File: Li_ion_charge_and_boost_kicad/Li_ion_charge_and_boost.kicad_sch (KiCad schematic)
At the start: 10 parts, among them U1 TP4056, U2 Type_C_6_pin

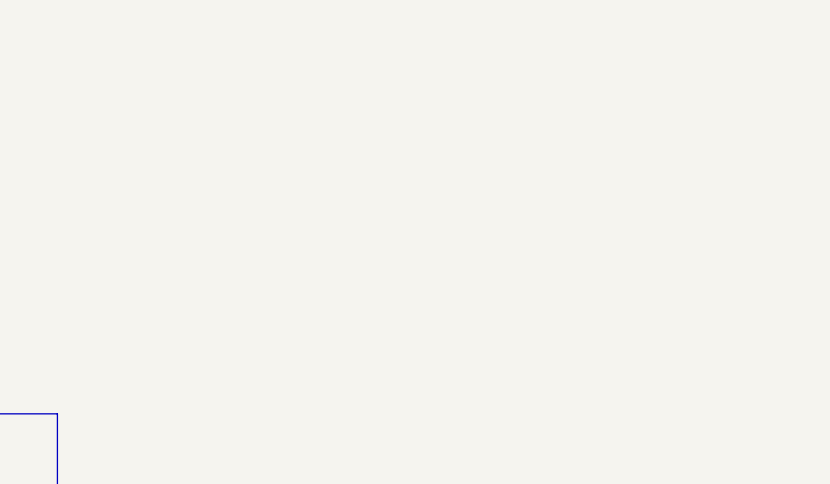
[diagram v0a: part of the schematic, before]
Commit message: DW01A included
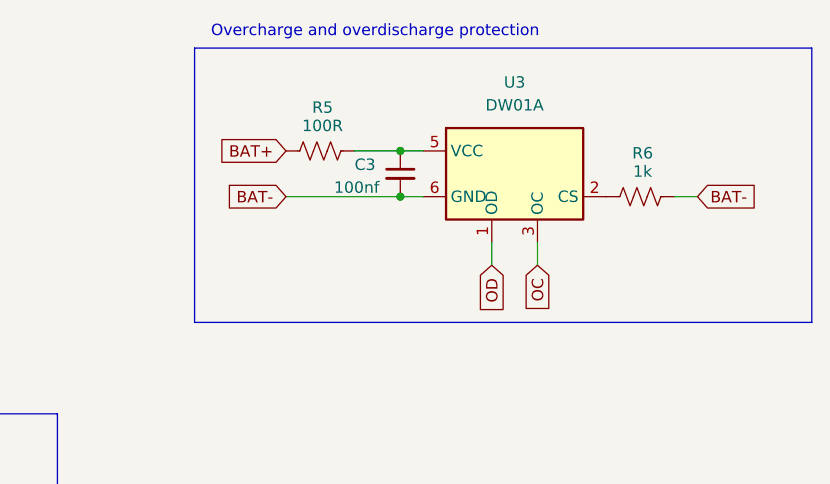
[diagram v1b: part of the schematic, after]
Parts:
- added C3: 100nf, symbol Device:C_Small
- added R5: 100R, symbol Device:R_US
- added R6: 1k, symbol Device:R_US
- added U3: DW01A, Package_TO_SOT_SMD:SOT-23-6, symbol Battery_Management:DW01A
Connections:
- net BAT+: now also R5.1
- new net: C3.1, R5.2, U3.5 (VCC)
- new net: R6.1, U3.2 (CS)
- new net BAT-: C3.2, R6.2, U3.6 (GND)
- new net OC: U3.3 (OC)
- new net OD: U3.1 (OD)
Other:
- note added: "Overcharge and overdischarge protection"

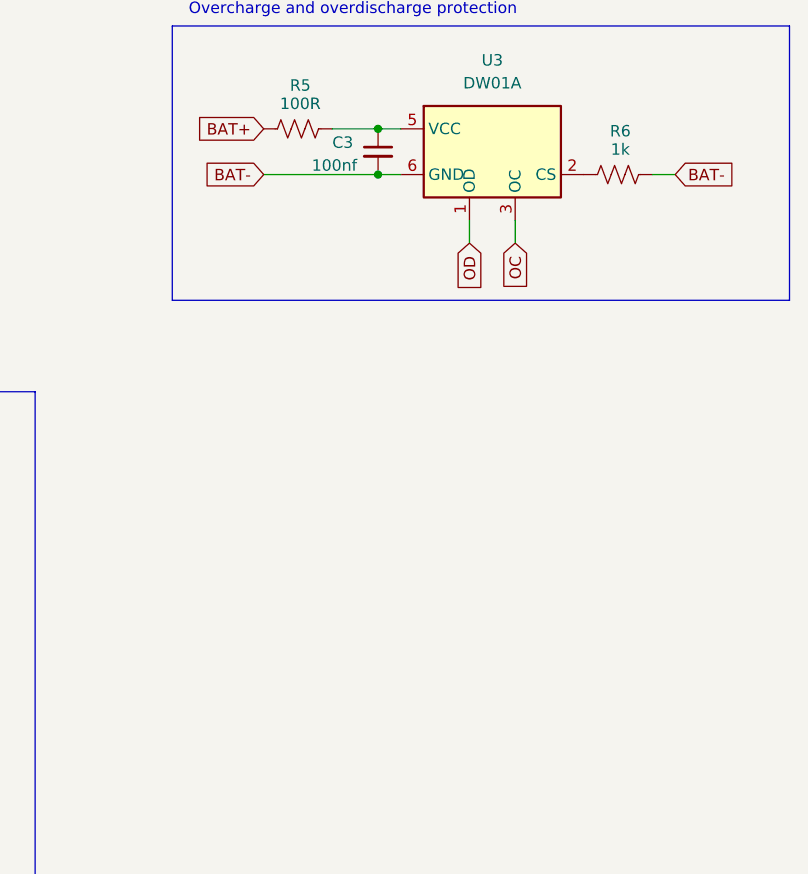
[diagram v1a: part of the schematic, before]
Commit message: Mosfet switch added
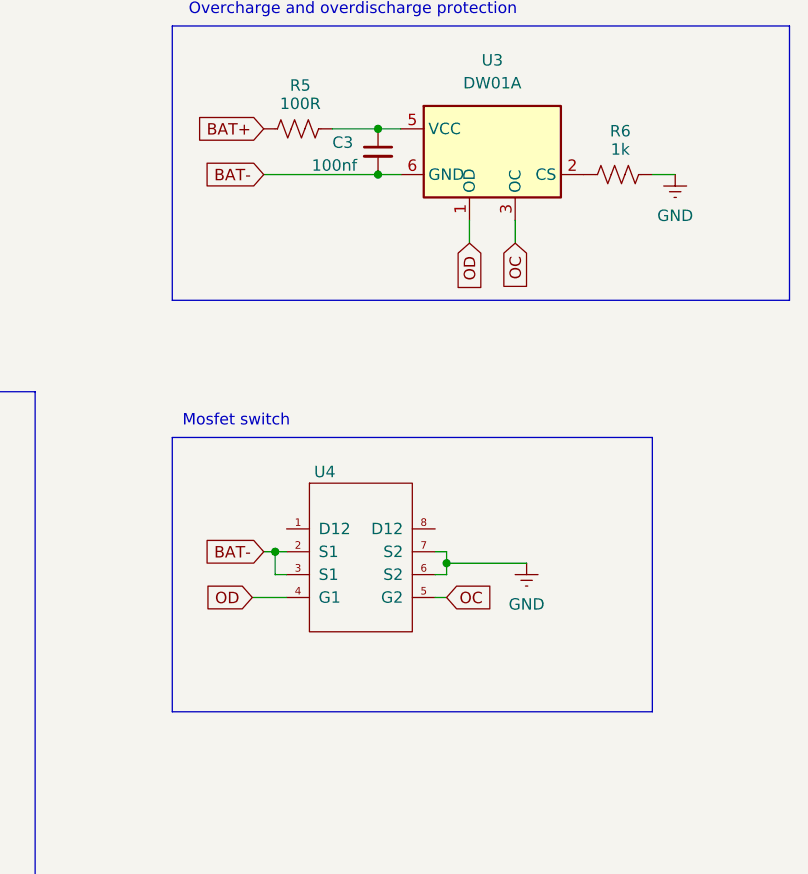
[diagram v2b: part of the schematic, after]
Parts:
- added U4: ~, symbol My_Library:FS8205A
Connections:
- net BAT-: now also U4.2 (S1), U4.3 (S1); no longer R6.2
- net GND: now also R6.2, U4.6 (S2), U4.7 (S2)
- net OC: now also U4.5 (G2)
- net OD: now also U4.4 (G1)
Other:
- note added: "Mosfet switch"

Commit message: Li ion charger completed
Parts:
- U4: footprint (none) -> My Library:FS8205A
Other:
- note added: "Li ion Charger"
- moved on the sheet: C3, R5, R6, U2, U3, U4

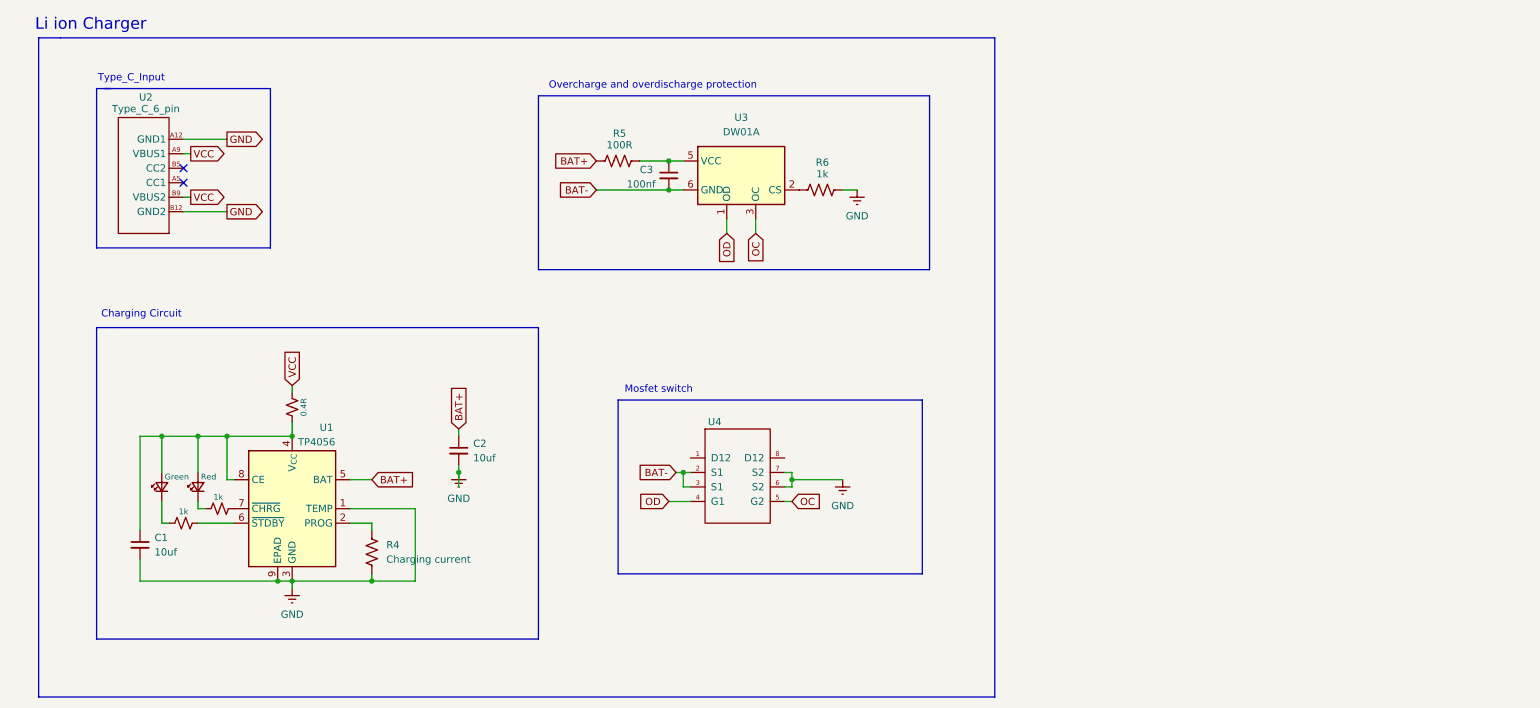
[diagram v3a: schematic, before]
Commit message: Boost converter added
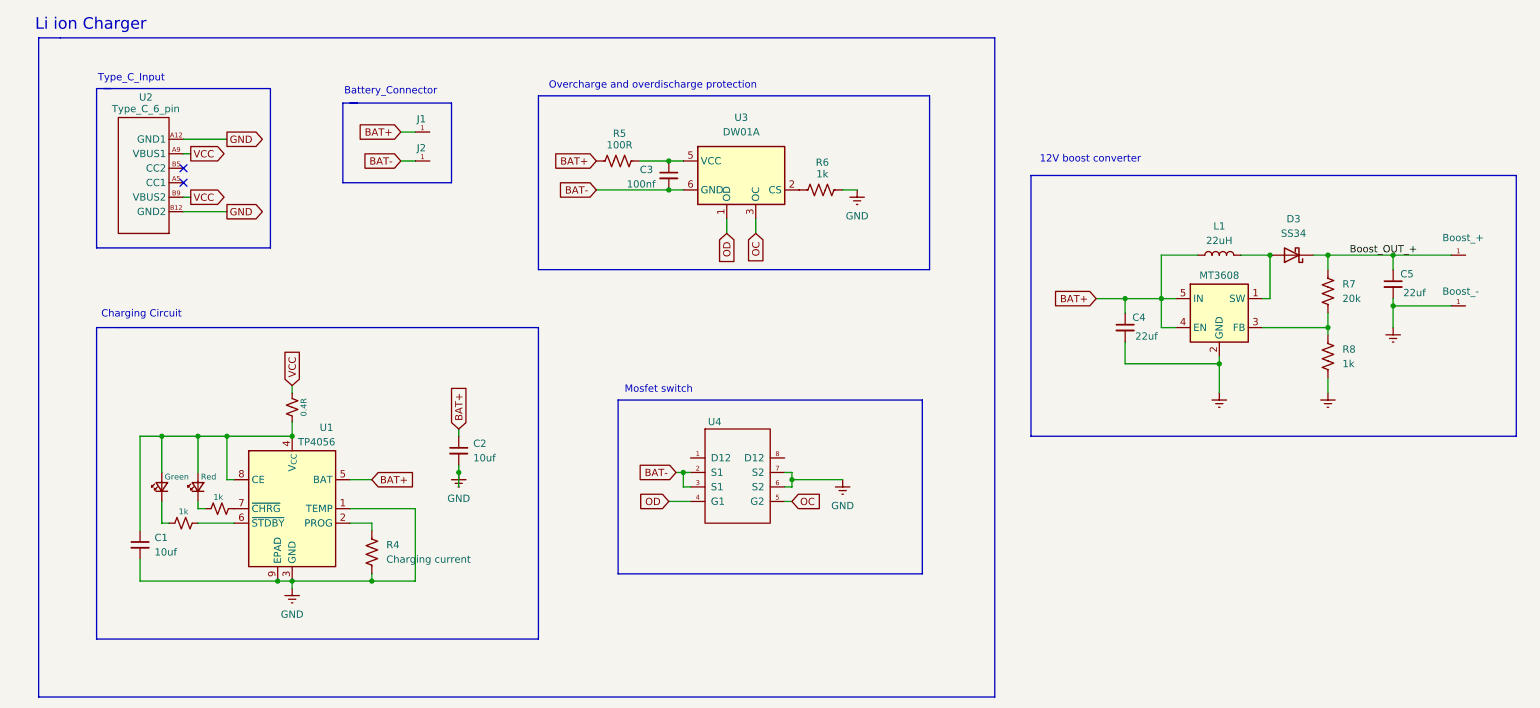
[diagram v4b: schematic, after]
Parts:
- added C4, C5: 22uf, symbol Device:C_Small
- added D3: SS34, Diode_SMD:D_SMA, symbol Diode:SS34
- added J1, J2: ~, symbol My_Library:Power_Connector
- added J3: Boost_+, symbol My_Library:Power_Connector
- added J4: Boost_-, symbol My_Library:Power_Connector
- added L1: 22uH, symbol Device:L
- added R7: 20k, symbol Device:R_US
- added R8: 1k, symbol Device:R_US
- added U5: MT3608, Package_TO_SOT_SMD:SOT-23-6, symbol Regulator_Switching:MT3608
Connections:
- net BAT+: now also C4.1, J1.1, L1.1, U5.4 (EN), U5.5 (IN)
- net BAT-: now also J2.1
- net GND: now also C4.2, C5.2, J4.1, R8.2, U5.2 (GND)
- new net: R7.2, R8.1, U5.3 (FB)
- new net: D3.2 (A), L1.2, U5.1 (SW)
- new net Boost_OUT_+: C5.1, D3.1 (K), J3.1, R7.1
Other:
- note added: "12V boost converter"
- note added: "Battery_Connector"

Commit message: Charging current and Inductor yet to confirm
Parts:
- R4: value Charging current -> 1.2k ( charging Current )
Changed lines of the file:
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@@
 	)
 	(junction
-		(at 93.98 105.41)
-		(diameter 0)
-		(color 0 0 0 0)
-	)
-	(junction
 		(at 257.81 67.31)
 		(diameter 0)
@@
 	(wire
 		(pts
-			(xy 93.98 105.41) (xy 93.98 107.95)
-		)
-		(stroke
-			(width 0)
-			(type default)
-		)
-	)
-	(wire
-		(pts
 			(xy 93.98 97.79) (xy 93.98 99.06)
 		)
@@
 		(on_board yes)
 		(dnp no)
-		(fields_autoplaced yes)
 		(property "Reference" "R4"
 			(at 81.28 118.1099 0)
@@
 			)
 		)
-		(property "Value" "Charging current"
-			(at 81.28 120.6499 0)
+		(property "Value" "1.2k   ( charging Current )"
+			(at 81.026 120.65 0)
 			(effects
 				(font

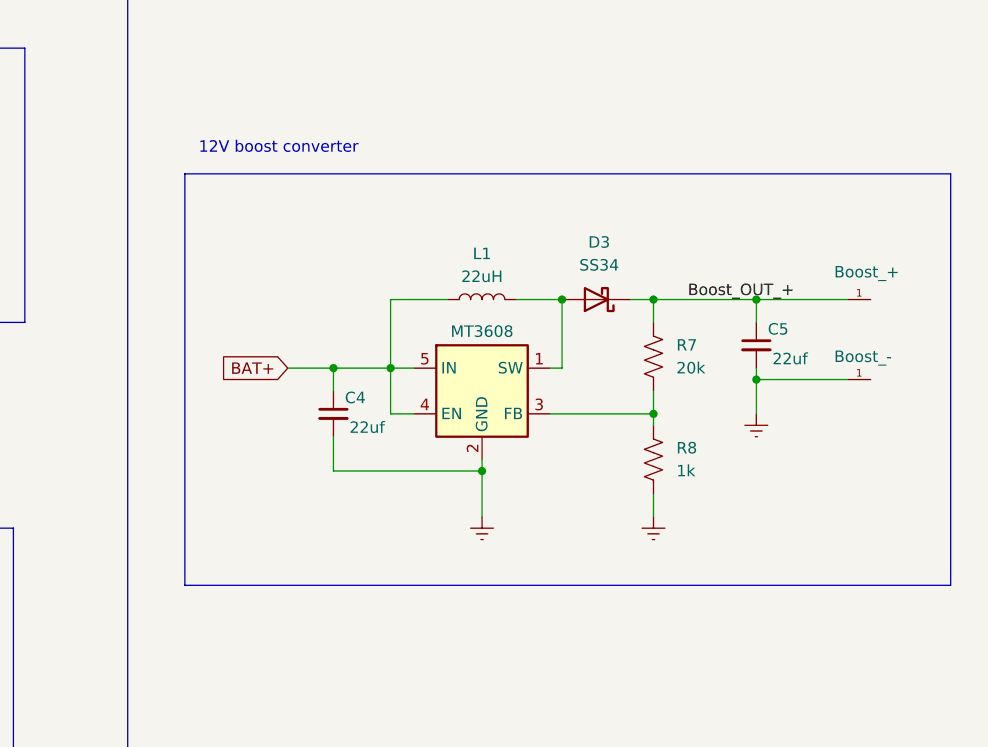
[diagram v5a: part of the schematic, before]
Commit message: switch input, microcontroller input and 2nd connector output
Switch to control the boost converter manually. Micorocontroller input to control automatically and 2nd output connector for more connections.
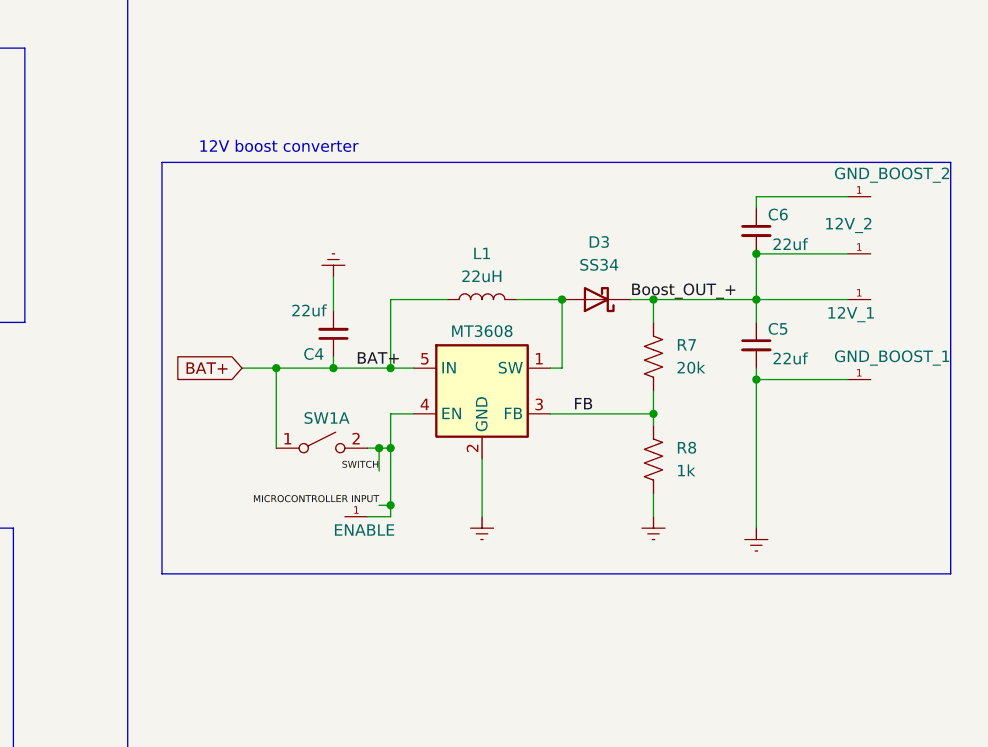
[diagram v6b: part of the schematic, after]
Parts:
- added C6: 22uf, symbol Device:C_Small
- added J5: ENABLE, symbol My_Library:Power_Connector
- added J6: 12V_2, symbol My_Library:Power_Connector
- added J7: GND_BOOST_2, symbol My_Library:Power_Connector
- added SW1: SW_DPST_x2, symbol Switch:SW_DPST_x2
- J3: value Boost_+ -> 12V_1
- J4: value Boost_- -> GND_BOOST_1
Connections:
- net BAT+: now also SW1.1 (A); no longer U5.4 (EN)
- net Boost_OUT_+: now also C6.2, J6.1
- net FB: now reaches R7.2, R8.1, U5.3 (FB)
- new net: C6.1, J7.1
- new net MICROCONTROLLER INPUT: J5.1, SW1.2 (B), U5.4 (EN)
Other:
- moved on the sheet: C4

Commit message: Type_C_footprint modified
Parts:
- U2: footprint My Library:Type_C_6_Pin -> Library:Type_c_6_Pin_Horizontal_mount
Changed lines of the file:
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@@
 			)
 		)
-		(property "Footprint" "My Library:Type_C_6_Pin"
+		(property "Footprint" "Library:Type_c_6_Pin_Horizontal_mount"
 			(at 45.72 63.5 0)
 			(effects

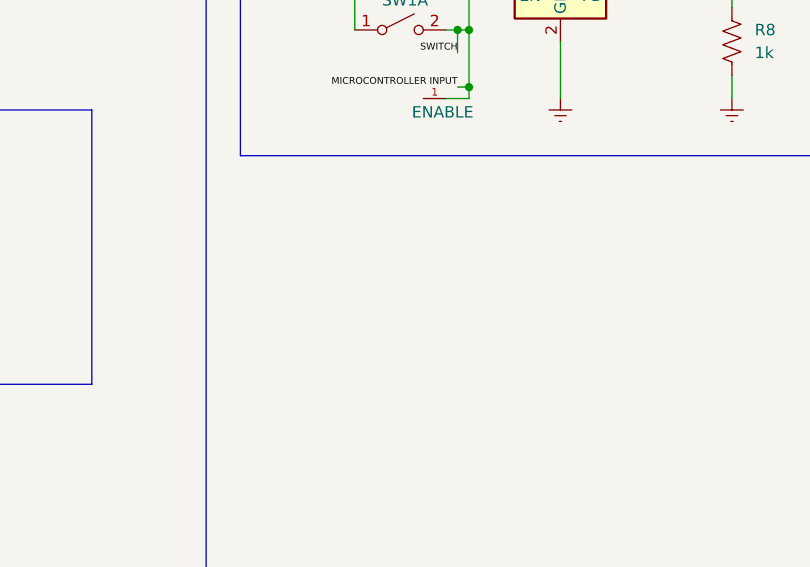
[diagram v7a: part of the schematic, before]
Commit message: Battery output to connector with switch
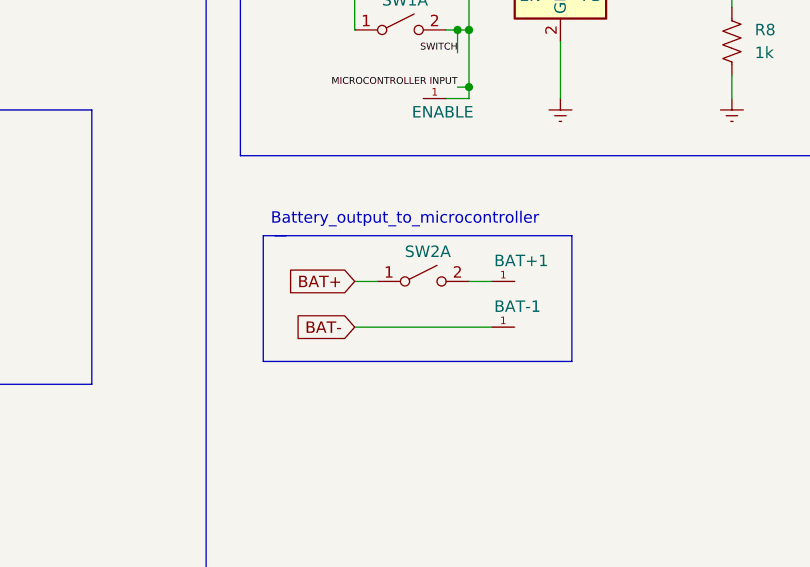
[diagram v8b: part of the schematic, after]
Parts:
- added BAT+1, BAT-1: ~, symbol My_Library:Power_Connector
- added SW2: SW_DPST_x2, symbol Switch:SW_DPST_x2
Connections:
- net BAT+: now also SW2.1 (A)
- net BAT-: now also BAT-1.1
- new net: BAT+1.1, SW2.2 (B)
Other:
- note added: "Battery_output_to_microcontroller"
